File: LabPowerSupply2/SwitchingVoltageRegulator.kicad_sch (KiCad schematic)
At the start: 17 parts

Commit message: Beautifing the Schematic
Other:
- moved on the sheet: C2_SVR1, C3_SVR1, C4_SVR1, C5_SVR1, L_SVR1, R2_SVR1, R31_SVR1, R32_SVR1, R41_SVR1, R42_SVR1, R5_SVR1, R6_SVR1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

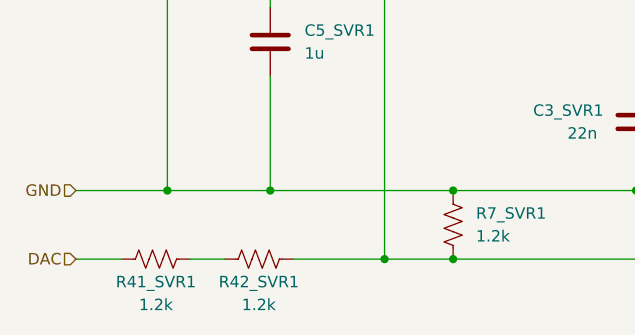
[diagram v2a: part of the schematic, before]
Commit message: Added plots for voltage and current error along with their data and scripts
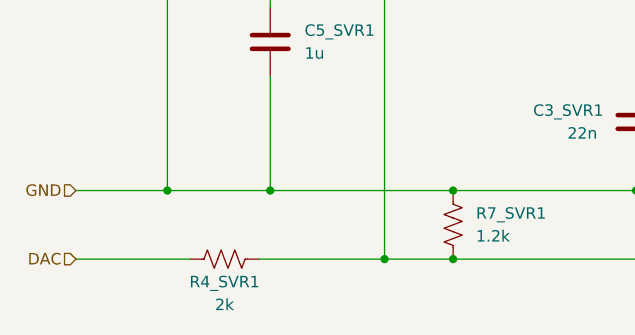
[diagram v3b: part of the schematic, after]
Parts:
- removed R42_SVR1: 1.2k, Resistor_SMD:R_0603_1608Metric, symbol Device:R_US
- R4_SVR1: renamed from R41_SVR1; value 1.2k -> 2k
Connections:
- net FeedBack: now also R4_SVR1.1
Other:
- moved on the sheet: R4_SVR1
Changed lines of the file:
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@@
   (paper "A4")
   (title_block
-    (date "2022-08-29")
-    (rev "1")
+    (date "2022-11-30")
+    (rev "2")
     (company "George Mason University")
     (comment 2 "linear regulator does as little work as possible.")
@@
     (stroke (width 0) (type default) (color 0 0 0 0))
   )
-  (wire (pts (xy 100.33 135.89) (xy 110.49 135.89))
-    (stroke (width 0) (type default) (color 0 0 0 0))
-  )
   (wire (pts (xy 144.78 92.71) (xy 140.97 92.71))
     (stroke (width 0) (type default) (color 0 0 0 0))
@@
     (stroke (width 0) (type default) (color 0 0 0 0))
   )
-  (wire (pts (xy 88.9 135.89) (xy 92.71 135.89))
+  (wire (pts (xy 96.52 135.89) (xy 110.49 135.89))
     (stroke (width 0) (type default) (color 0 0 0 0))
   )
@@
     (stroke (width 0) (type default) (color 0 0 0 0))
   )
-  (wire (pts (xy 76.2 135.89) (xy 81.28 135.89))
+  (wire (pts (xy 76.2 135.89) (xy 88.9 135.89))
     (stroke (width 0) (type default) (color 0 0 0 0))
   )
@@
     (pin "2")
   )
-  (symbol (lib_id "Device:R_US") (at 85.09 135.89 270) (unit 1)
+  (symbol (lib_id "Device:R_US") (at 92.71 135.89 270) (unit 1)
     (in_bom yes) (on_board yes)
-    (property "Reference" "R41_SVR1" (id 0) (at 85.09 138.43 90))
-    (property "Value" "1.2k" (id 1) (at 85.09 140.97 90))
-    (property "Footprint" "Resistor_SMD:R_0603_1608Metric" (id 2) (at 84.836 136.906 90)
-      (effects (font (size 1.27 1.27)) hide)
-    )
-    (property "Datasheet" "~" (id 3) (at 85.09 135.89 0)
+    (property "Reference" "R4_SVR1" (id 0) (at 92.71 138.43 90))
+    (property "Value" "2k" (id 1) (at 92.71 140.97 90))
+    (property "Footprint" "Resistor_SMD:R_0603_1608Metric" (id 2) (at 92.456 136.906 90)
+      (effects (font (size 1.27 1.27)) hide)
+    )
+    (property "Datasheet" "~" (id 3) (at 92.71 135.89 0)
       (effects (font (size 1.27 1.27)) hide)
     )
@@
       (effects (font (size 1.27 1.27)) hide)
     )
-    (pin "1")
-    (pin "2")
-  )
-  (symbol (lib_id "Device:R_US") (at 96.52 135.89 270) (unit 1)
-    (in_bom yes) (on_board yes)
-    (property "Reference" "R42_SVR1" (id 0) (at 96.52 138.43 90))
-    (property "Value" "1.2k" (id 1) (at 96.52 140.97 90))
-    (property "Footprint" "Resistor_SMD:R_0603_1608Metric" (id 2) (at 96.266 136.906 90)
-      (effects (font (size 1.27 1.27)) hide)
-    )
-    (property "Datasheet" "~" (id 3) (at 96.52 135.89 0)
-      (effects (font (size 1.27 1.27)) hide)
-    )
